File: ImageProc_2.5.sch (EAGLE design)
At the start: 115 parts, among them IC1 XC61GC3002HR-G, IC10 AT45DB642D-CNU, IC2 MIC5335-SPYMT, IC3 MIC5335-JGYMT, IC4 DSPIC33FJ128MC706A, IC5 AT86RF233-ZU, IC6 LTC6088, IC7 DRV8833RTY, IC8 DRV8833RTY, IC9 MPU-6000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

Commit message: Motor section mostly complete. Board expanded. PIC passives mostly complete.
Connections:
- net 3.3V: now also R16.2
- net V_BATT: no longer R16.2
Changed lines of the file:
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@@
-</segment>
-<segment>
-<pinref part="U$1" gate="G$1" pin="3.3V"/>
-<pinref part="R16" gate="G$1" pin="2"/>
-<wire x1="231.14" y1="124.46" x2="231.14" y2="121.92" width="0.1524" layer="91"/>
 </segment>
 <segment>
@@
 <junction x="121.92" y="27.94"/>
 </segment>
+<segment>
+<pinref part="U$1" gate="G$1" pin="3.3V"/>
+<pinref part="R16" gate="G$1" pin="2"/>
+<wire x1="231.14" y1="124.46" x2="231.14" y2="121.92" width="0.1524" layer="91"/>
+</segment>
 </net>

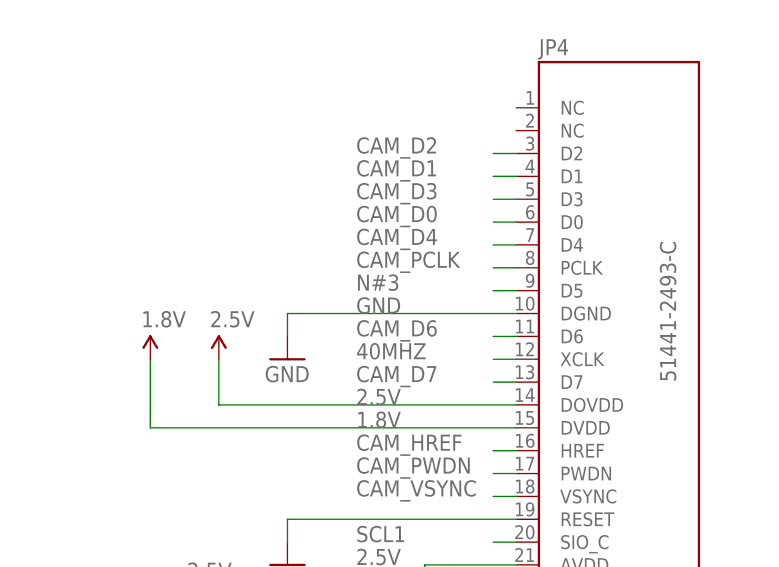
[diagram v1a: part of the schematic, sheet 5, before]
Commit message: PIC and radio vias added. Partial camera route.
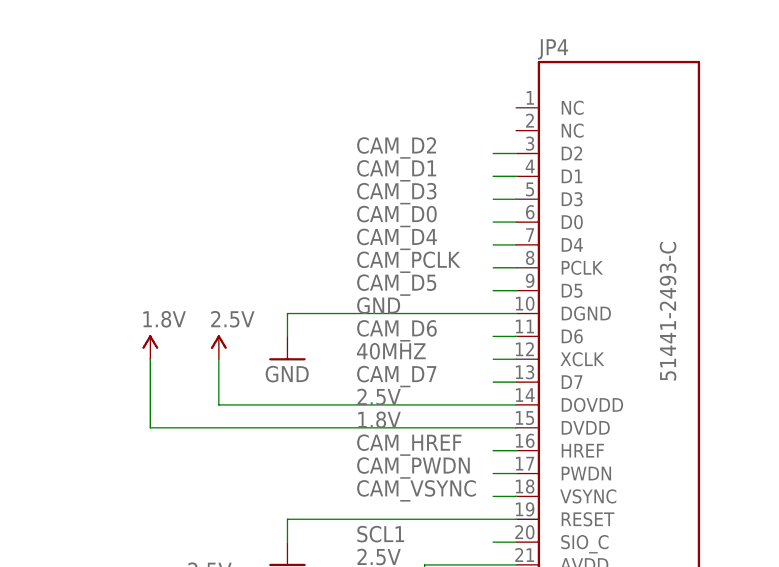
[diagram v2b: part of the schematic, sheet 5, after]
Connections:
- removed net N#3: JP4.D5
- net CAM_D5: now also JP4.D5
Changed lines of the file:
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@@
-</segment>
-</net>
-<net name="SDI1" class="0">
-<segment>
-<label x="66.04" y="111.76" size="1.778" layer="95"/>
-<pinref part="IC5" gate="S" pin="MISO"/>
-<wire x1="86.36" y1="111.76" x2="88.9" y2="111.76" width="0.1524" layer="91"/>
 </segment>
 </net>
@@
 <pinref part="C22" gate="G$1" pin="2"/>
 <wire x1="73.66" y1="25.4" x2="73.66" y2="22.86" width="0.1524" layer="91"/>
+</segment>
+</net>
+<net name="SDI1" class="0">
+<segment>
+<label x="66.04" y="111.76" size="1.778" layer="95"/>
+<pinref part="IC5" gate="S" pin="MISO"/>
+<wire x1="86.36" y1="111.76" x2="88.9" y2="111.76" width="0.1524" layer="91"/>
 </segment>
 </net>
@@
 </segment>
 </net>
-<net name="N#3" class="0">
+<net name="CAM_D5" class="0">
 <segment>
 <pinref part="JP4" gate="G$1" pin="D5"/>

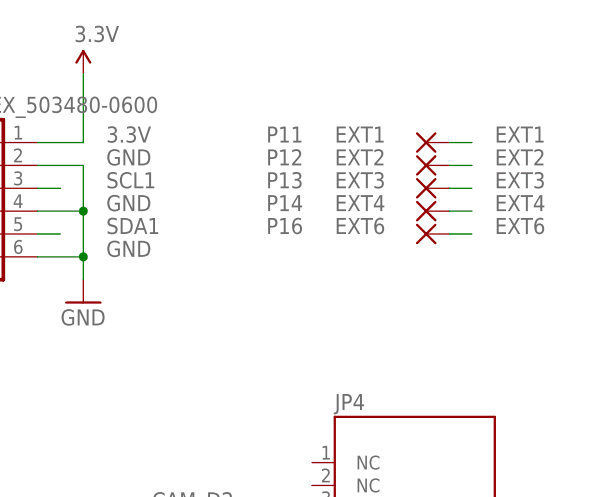
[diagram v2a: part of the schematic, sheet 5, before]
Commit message: Added anti-aliasing filter values (not sure how I missed those). Renamed external pins.
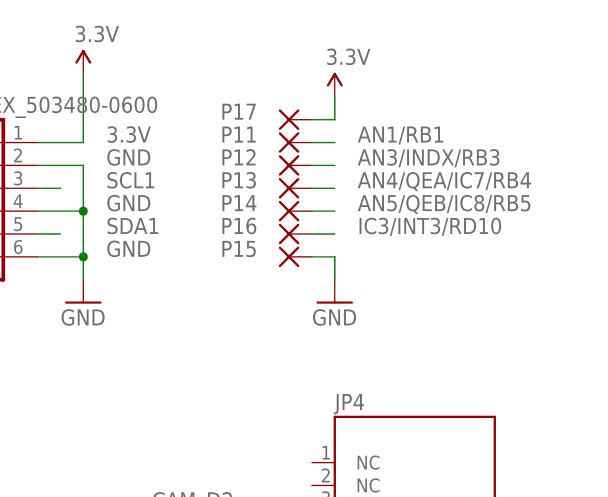
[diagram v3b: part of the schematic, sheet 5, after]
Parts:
- added P15, P17: EXT5, wirepad:SMD2
- C41, C42, C44: value (none) -> 2.2nF
- C43: value xnF -> 2.2nF
- P16: value EXT6 -> EXT5
- R29, R30, R31, R32: value (none) -> 1k
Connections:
- net EXT1 renamed AN1/RB1
- net EXT2 renamed AN3/INDX/RB3
- net EXT3 renamed AN4/QEA/IC7/RB4
- net EXT4 renamed AN5/QEB/IC8/RB5
- net EXT6 renamed IC3/INT3/RD10
- net 3.3V: now also P17.P
- net GND: now also P15.P
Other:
- moved on the sheet: P11, P12, P13, P14, P16

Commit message: ImageProc 2.5 Rev. A
Final silk screen and manufacturing modifications. Submitted for
prototype manufacturing on 7/26/2012.

ImageProc 2.5 updates the ImageProc with several new features and updated
silicon, while focusing on on enhanced manufacturability and ease of
modification. Software revisions to the octoroach and imageproc-lib codebases
are forthcoming.

Process/Manufacturing
* Changed from 2- to 4-layer process for routing and modificiation flexibility
* Functional units consolidated and rearranged for better isolation
* All ICs now on top side, (almost) all passives on bottom
* 6 mil trace/space for cheaper manufacturing processes in the prototyping
  stage
* Plane pours on all layers. Stack-up is Ground/Ground/Power/Ground. Signals
  run in all layers.
* All-new normalized part footprints, schematic symbols, and silk screen.
* Schematic now uses 5 sheets for enhanced readability. A non-free EagleCAD
  license is now required to view the files.
* A 10 mil tKeepout/bKeepout margin is now enforced at the boundaries of the
  board to ensure that the pick-and-place machine can reach all pads when the
  board is clamped into the board cradle.
* Many nets have been added and others renamed for clarification
* Much more conservative standards for component spacing

Power
* Panasonic MN13822-L voltage supervisor replaced with Torex XC61GC3002HR-G
  because the MN13822 has been discontinued
* Micrel MIC5320-JGYML 1.8/2.5 V regulator replaced with MIC5335-JGYMT
  because the MIC5320 is no longer available from suppliers.

Microcontroller
* Many pins have been relocated to make room for new features.
* Added bypass capacitors for each VDD/VSS pair and a filtering inductor
  to the VDD/AVDD connection, according to Microchip's recommendations

Radio
* ZigBee radio updated from Atmel AT86RF233 to the Atmel AT86RF233, which
  presents an identical electronic and software interface, but with silicon
  for an additional +1 dBm of transmit power
* Replaced ECS ECS-2033-160 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
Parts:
- renumbered P15 to GND, P17 to 3.3V
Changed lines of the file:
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@@
 <attributes>
 <attribute name="AUTHOR" value="Ryan Julian (ryanjulian@berkeley.edu)"/>
-<attribute name="REVISION" value="1"/>
+<attribute name="NAME" value="ImageProc 2.5"/>
+<attribute name="REVISION" value="A"/>
 <attribute name="YEAR" value="2012"/>
 </attributes>
@@
 <part name="GND33" library="biomimetic" deviceset="GND" device=""/>
 <part name="GND46" library="biomimetic" deviceset="GND" device=""/>
-<part name="P15" library="wirepad" deviceset="SMD2" device="" value="EXT5"/>
-<part name="P17" library="wirepad" deviceset="SMD2" device="" value="EXT5"/>
+<part name="GND" library="wirepad" deviceset="SMD2" device="" value="EXT5"/>
+<part name="3.3V" library="wirepad" deviceset="SMD2" device="" value="EXT5"/>
 <part name="P+1" library="biomimetic" deviceset="3.3V" device=""/>
 <part name="GND24" library="biomimetic" deviceset="GND" device=""/>
@@
 <attribute name="NAME" x="205.74" y="160.02" size="1.778" layer="95"/>
 </instance>
-<instance part="P15" gate="1" x="213.36" y="157.48" smashed="yes">
+<instance part="GND" gate="1" x="213.36" y="157.48" smashed="yes">
 <attribute name="NAME" x="205.74" y="157.48" size="1.778" layer="95"/>
 </instance>
-<instance part="P17" gate="1" x="213.36" y="172.72" smashed="yes">
+<instance part="3.3V" gate="1" x="213.36" y="172.72" smashed="yes">
 <attribute name="NAME" x="205.74" y="172.72" size="1.778" layer="95"/>
 </instance>
@@
 </segment>
 <segment>
-<pinref part="P15" gate="1" pin="P"/>
+<pinref part="GND" gate="1" pin="P"/>
 <pinref part="GND24" gate="1" pin="GND"/>
 <wire x1="215.9" y1="157.48" x2="218.44" y2="157.48" width="0.1524" layer="91"/>
@@
 </segment>
 <segment>
-<pinref part="P17" gate="1" pin="P"/>
+<pinref part="3.3V" gate="1" pin="P"/>
 <wire x1="215.9" y1="172.72" x2="218.44" y2="172.72" width="0.1524" layer="91"/>
 <pinref part="P+1" gate="G$1" pin="3.3V"/>
